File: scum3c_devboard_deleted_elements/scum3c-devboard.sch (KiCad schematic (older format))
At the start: 7 parts, among them U9AB1 MPU-9250

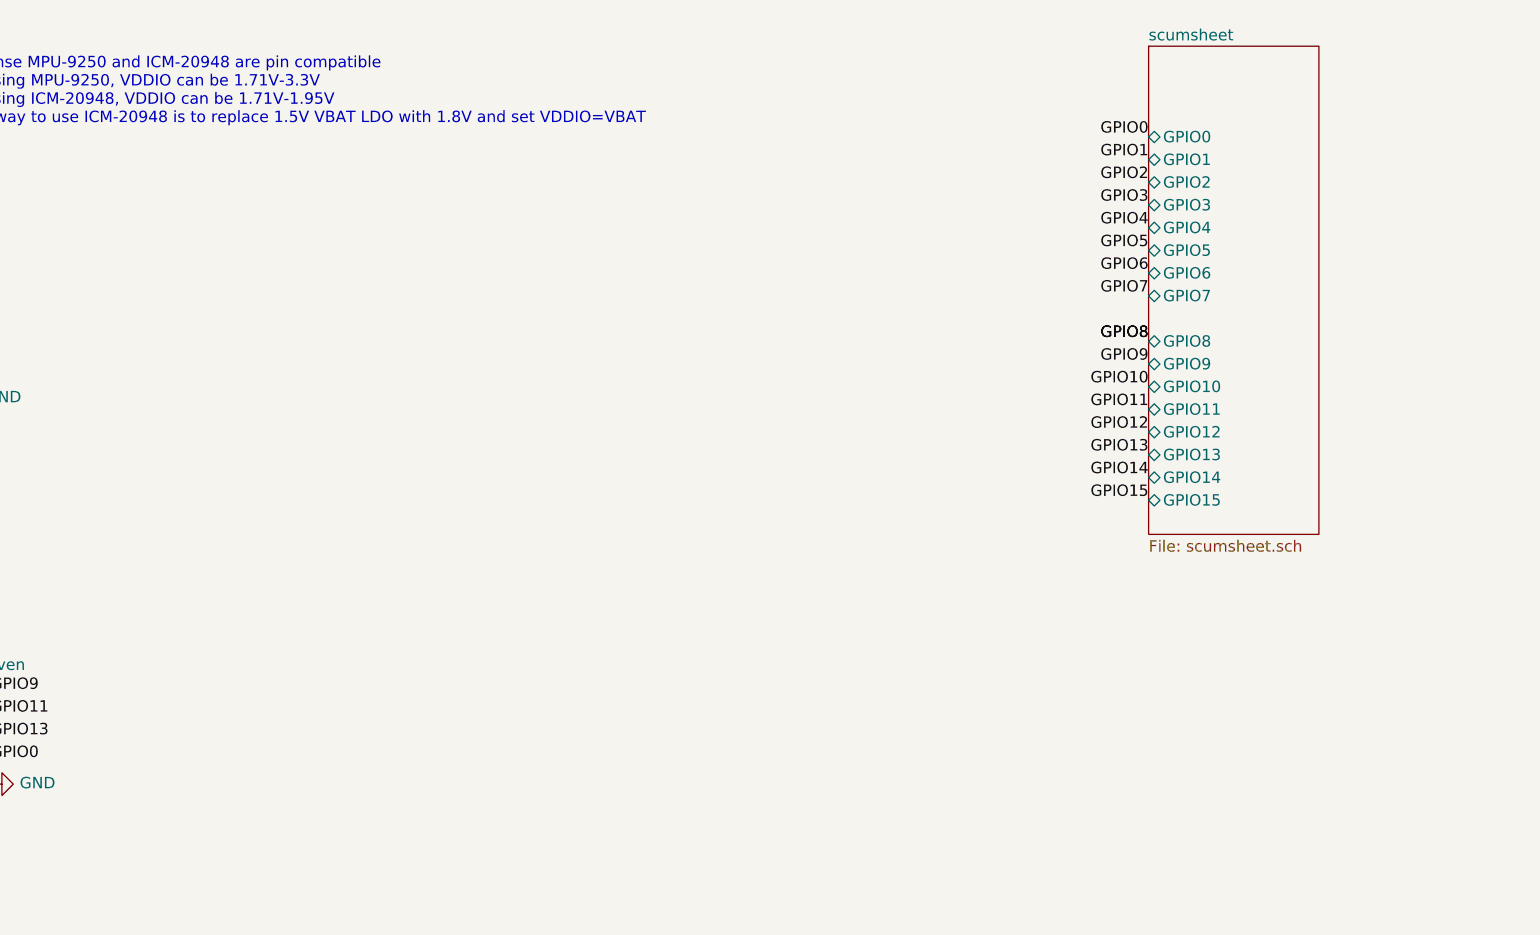
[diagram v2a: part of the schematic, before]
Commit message: added LED
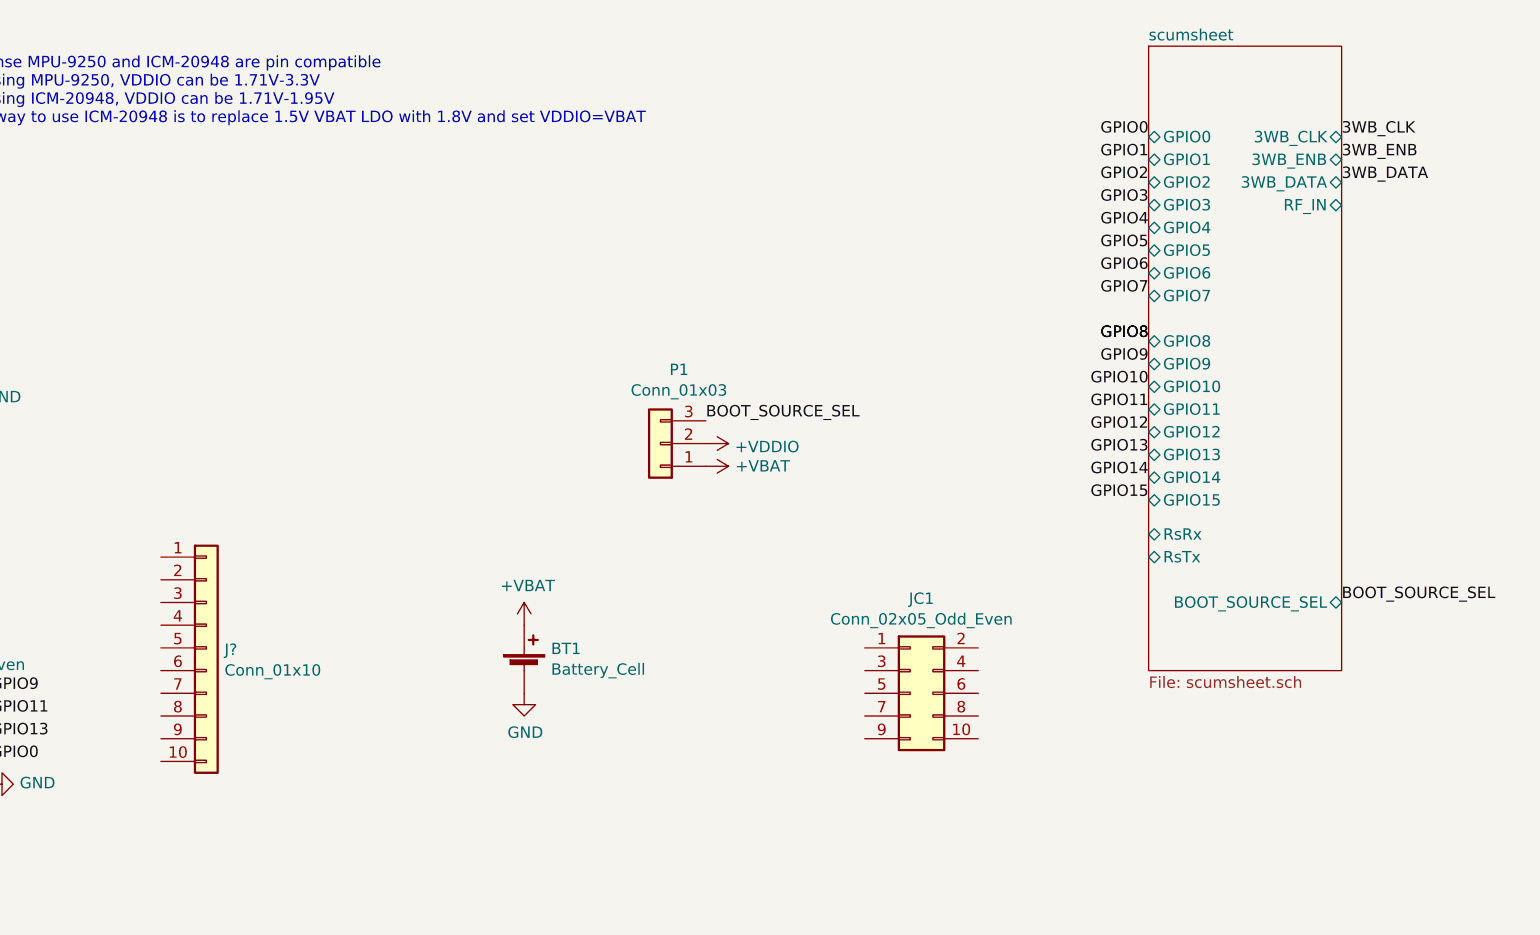
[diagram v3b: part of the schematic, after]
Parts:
- added BT1: Battery_Cell, SamacSys_Parts:2986, symbol Device:Battery_Cell
- added J?: Conn_01x10, symbol Connector_Generic:Conn_01x10
- added JC1: Conn_02x05_Odd_Even, Connector_PinHeader_2.54mm:PinHeader_2x05_P2.54mm_Vertical, symbol Connector_Generic:Conn_02x05_Odd_Even
- added P1: Conn_01x03, Connector_PinHeader_2.54mm:PinHeader_1x03_P2.54mm_Vertical, symbol Connector_Generic:Conn_01x03
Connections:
- net +VBAT: now also BT1.1 (+), P1.1 (Pin_1)
- net +VDDIO: now also P1.2 (Pin_2)
- net GND: now also BT1.2 (-)
- new net BOOT_SOURCE_SEL: P1.3 (Pin_3)
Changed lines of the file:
@@
 	1    0    0    -1
 $EndComp
-Text Label 1750 3650 2    50   ~ 0
-GPIO2
-Text Label 2250 3650 0    50   ~ 0
-GPIO1
-Text Label 1750 3750 2    50   ~ 0
-GPIO4
-Text Label 1750 3850 2    50   ~ 0
-GPIO6
-Text Label 1750 3950 2    50   ~ 0
-GPIO8
-Text Label 2250 3950 0    50   ~ 0
-GPIO7
-Text Label 2250 3850 0    50   ~ 0
-GPIO5
-Text Label 2250 3750 0    50   ~ 0
-GPIO3
 Text Label 2950 3650 2    50   ~ 0
 GPIO10
@@
 GPIO15
 $Sheet
-S 8550 800  750  2150
+S 8550 800  850  2750
 U 5F3B1D81
 F0 "scumsheet" 50
@@
 F16 "GPIO15" B L 8550 2800 50
 F17 "GPIO0" B L 8550 1200 50
+F18 "3WB_CLK" B R 9400 1200 50
+F19 "3WB_ENB" B R 9400 1300 50
+F20 "3WB_DATA" B R 9400 1400 50
+F21 "RF_IN" B R 9400 1500 50
+F22 "RsTx" B L 8550 3050 50
+F23 "RsRx" B L 8550 2950 50
+F24 "BOOT_SOURCE_SEL" B R 9400 3250 50
 $EndSheet
 $Comp
@@
 Text Notes 5150 6450 0    50   ~ 0
 hope this is the right component for voltage protection
+Text Label 9400 1200 0    50   ~ 0
+3WB_CLK
+Text Label 9400 1300 0    50   ~ 0
+3WB_ENB
+Text Label 9400 1400 0    50   ~ 0
+3WB_DATA
+$Comp
+L power:GND #PWR0120
+U 1 1 5F7C4691
+P 5800 3650
+F 0 "#PWR0120" H 5800 3400 50  0001 C CNN
+F 1 "GND" H 5805 3477 50  0000 C CNN
+F 2 "" H 5800 3650 50  0001 C CNN
+F 3 "" H 5800 3650 50  0001 C CNN
+	1    5800 3650
+	1    0    0    -1
+$EndComp
+$Comp
+L draft1library:+VBAT #PWR0121
+U 1 1 5F7C4697
+P 5800 3350
+F 0 "#PWR0121" H 5800 3200 50  0001 C CNN
+F 1 "+VBAT" H 5815 3523 50  0000 C CNN
+F 2 "" H 5800 3350 50  0001 C CNN
+F 3 "" H 5800 3350 50  0001 C CNN
+	1    5800 3350
+	1    0    0    -1
+$EndComp
+$Comp
+L Device:Battery_Cell BT1
+U 1 1 5F7C469D
+P 5800 3550
+F 0 "BT1" H 5918 3646 50  0000 L CNN
+F 1 "Battery_Cell" H 5918 3555 50  0000 L CNN
+F 2 "SamacSys_Parts:2986" V 5800 3610 50  0001 C CNN
+F 3 "~" V 5800 3610 50  0001 C CNN
+	1    5800 3550
+	1    0    0    -1
+$EndComp
+$Comp
+L draft1library:+VBAT #PWR?
+U 1 1 5F7B958D
+P 6600 2650
+AR Path="/5F3B1D81/5F7B958D" Ref="#PWR?"  Part="1"
+AR Path="/5F41418C/5F7B958D" Ref="#PWR?"  Part="1"
+AR Path="/5F414989/5F7B958D" Ref="#PWR?"  Part="1"
+AR Path="/5F7B958D" Ref="#PWR0109"  Part="1"
+F 0 "#PWR0109" H 6600 2500 50  0001 C CNN
+F 1 "+VBAT" V 6600 2900 50  0000 C CNN
+F 2 "" H 6600 2650 50  0001 C CNN
+F 3 "" H 6600 2650 50  0001 C CNN
+	1    6600 2650
+	0    1    1    0
+$EndComp
+Text Label 6600 2450 0    50   ~ 0
+BOOT_SOURCE_SEL
+$Comp
+L Connector_Generic:Conn_01x03 P?
+U 1 1 5F7B9594
+P 6400 2550
+AR Path="/5F3B1D81/5F7B9594" Ref="P?"  Part="1"
+AR Path="/5F7B9594" Ref="P1"  Part="1"
+F 0 "P1" H 6318 2225 50  0000 C CNN
+F 1 "Conn_01x03" H 6318 2316 50  0000 C CNN
+F 2 "Connector_PinHeader_2.54mm:PinHeader_1x03_P2.54mm_Vertical" H 6400 2550 50  0001 C CNN
+F 3 "~" H 6400 2550 50  0001 C CNN
+	1    6400 2550
+	-1   0    0    1
+$EndComp
+$Comp
+L draft1library:+VDDIO #PWR?
+U 1 1 5F7B959A
+P 6600 2550
+AR Path="/5F3B1D81/5F7B959A" Ref="#PWR?"  Part="1"
+AR Path="/5F7B959A" Ref="#PWR0110"  Part="1"
+F 0 "#PWR0110" H 6600 2400 50  0001 C CNN
+F 1 "+VDDIO" V 6615 2678 50  0000 L CNN
+F 2 "" H 6600 2550 50  0001 C CNN
+F 3 "" H 6600 2550 50  0001 C CNN
+	1    6600 2550
+	0    1    1    0
+$EndComp
+Text Label 9400 3250 0    50   ~ 0
+BOOT_SOURCE_SEL
+$Comp
+L Connector_Generic:Conn_02x05_Odd_Even JC1
+U 1 1 5F7BA02A
+P 7500 3650
+F 0 "JC1" H 7550 4067 50  0000 C CNN
+F 1 "Conn_02x05_Odd_Even" H 7550 3976 50  0000 C CNN
+F 2 "Connector_PinHeader_2.54mm:PinHeader_2x05_P2.54mm_Vertical" H 7500 3650 50  0001 C CNN
+F 3 "~" H 7500 3650 50  0001 C CNN
+	1    7500 3650
+	1    0    0    -1
+$EndComp
+$Comp
+L Connector_Generic:Conn_01x10 J?
+U 1 1 5F7BC634
+P 4400 3450
+F 0 "J?" H 4480 3442 50  0000 L CNN
+F 1 "Conn_01x10" H 4480 3351 50  0000 L CNN
+F 2 "" H 4400 3450 50  0001 C CNN
+F 3 "~" H 4400 3450 50  0001 C CNN
+	1    4400 3450
+	1    0    0    -1
+$EndComp
+Text Label 2250 3750 0    50   ~ 0
+GPIO3
+Text Label 2250 3850 0    50   ~ 0
+GPIO5
+Text Label 2250 3950 0    50   ~ 0
+GPIO7
+Text Label 2250 3650 0    50   ~ 0
+GPIO1
+Text Label 1750 3950 2    50   ~ 0
+GPIO8
+Text Label 1750 3850 2    50   ~ 0
+GPIO6
+Text Label 1750 3750 2    50   ~ 0
+GPIO4
+Text Label 1750 3650 2    50   ~ 0
+GPIO2
 $EndSCHEMATC
